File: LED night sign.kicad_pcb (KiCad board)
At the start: 2 copper layers, 42.9 x 36.7 mm, 24 parts, among them Q1 MOSFET-NCH-2N7002PW, U1 ATtiny85-20P, U2 ATtiny85-20S

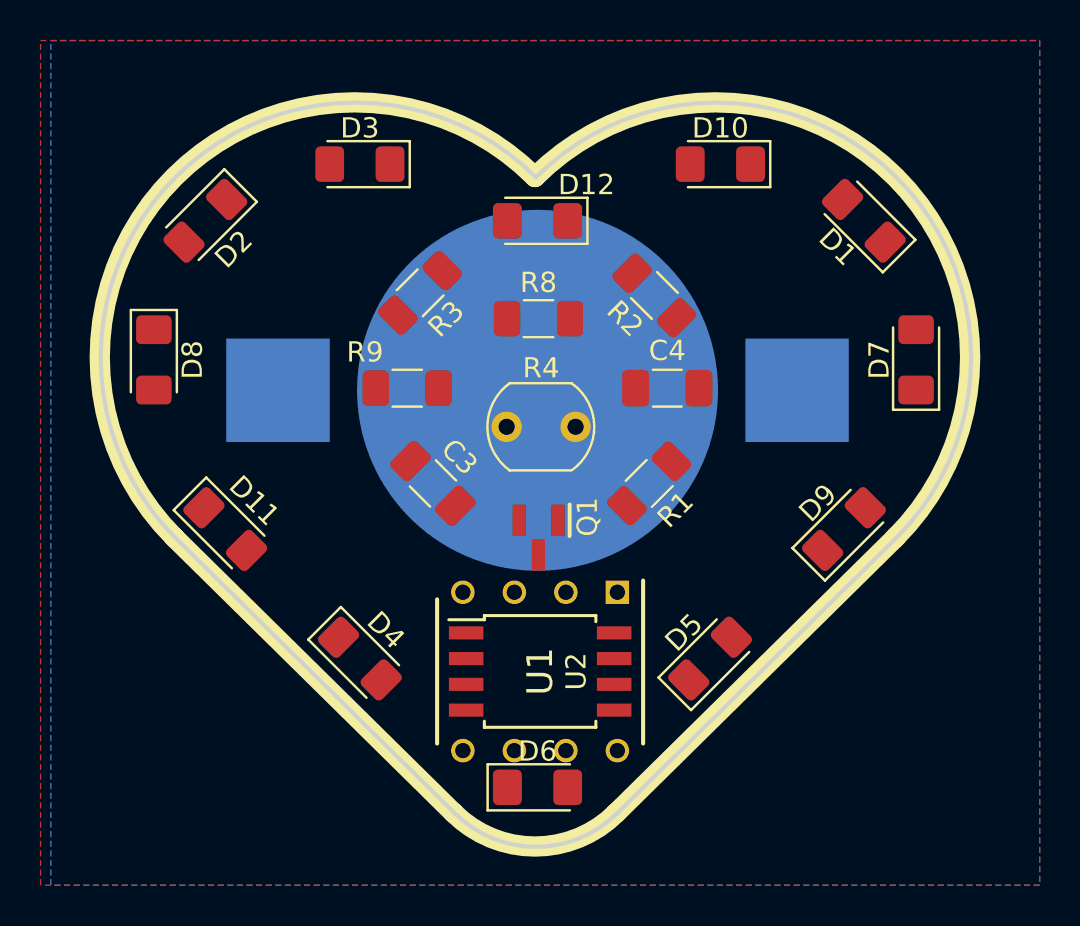
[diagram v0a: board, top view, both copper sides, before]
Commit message: moved components a bit down.
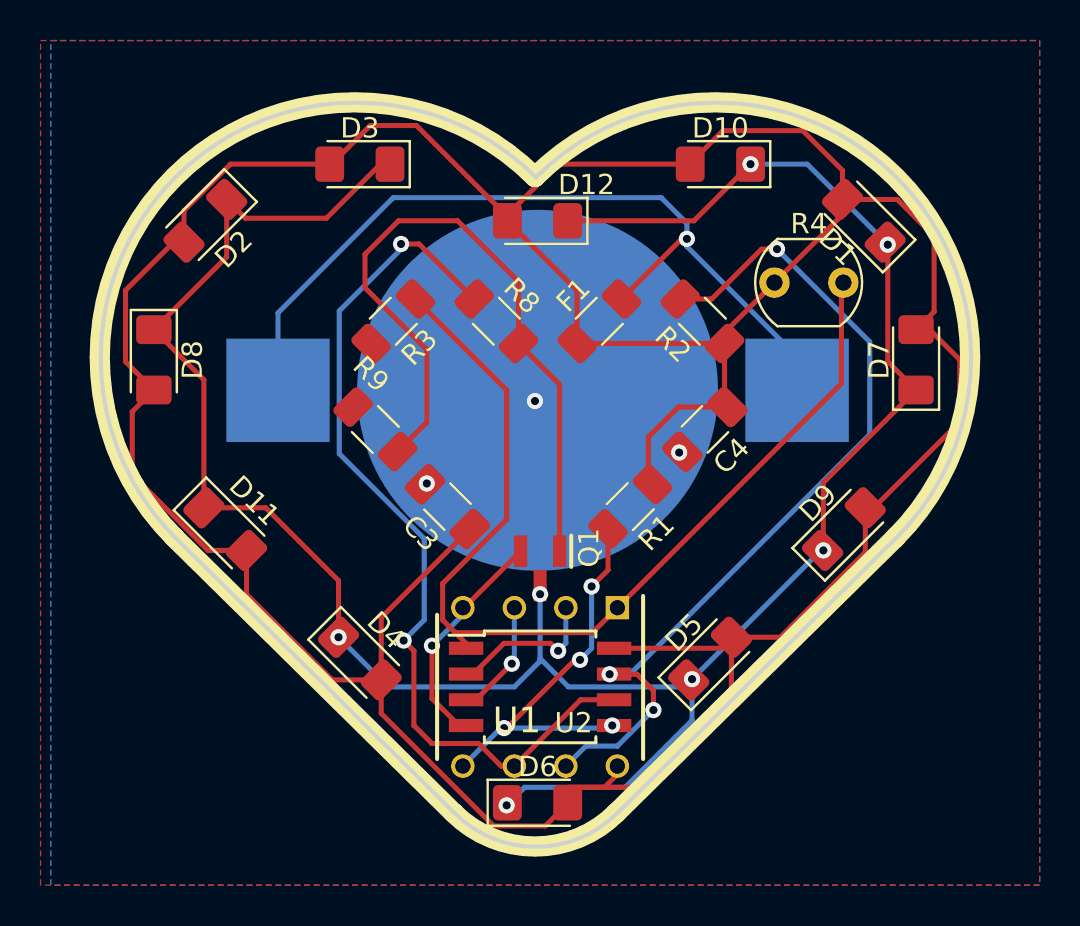
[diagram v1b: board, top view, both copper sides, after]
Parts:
- added F1: Fuse, Resistor_SMD:R_1206_3216Metric_Pad1.30x1.75mm_HandSolder, F.Cu at (153.0, 96.6)
- moved R4 15.0 mm to (161.7, 94.7)
- moved C4 2.75 mm to (158.2, 102.0), turned to -135 degrees
- moved R2 2.68 mm to (158.1, 96.6)
- moved R9 2.57 mm to (142.0, 102.0), turned to -45 degrees
- moved R8 2.08 mm to (148.0, 96.6), turned to 135 degrees
- moved R3 1.92 mm to (142.9, 96.6)
- moved Q1 1.53 mm to (150.1, 108.8)
- moved R1 1.48 mm to (154.6, 105.8)
- moved C3 1.35 mm to (145.5, 105.8), turned to 135 degrees
- moved D6 0.76 mm to (150.0, 120.4)
- moved U1 0.76 mm to (150.1, 114.7)
- moved U2 0.76 mm to (150.1, 114.7)
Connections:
- BT1 pad 1: +3V0 -> Net-(BT1-Pad1)
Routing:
- net +3V0: track 0.00 -> 186.0 mm
- net Net-(D1-Pad1): track 0.00 -> 119.5 mm, vias 0 -> 7
- net INTL: track 0.00 -> 50.0 mm
- net CTRLLED: track 0.00 -> 44.2 mm, vias 0 -> 2
- net PB2/SCL/SCK: track 0.00 -> 43.5 mm, vias 0 -> 3
- net Net-(BT1-Pad1): track 0.00 -> 41.8 mm, vias 0 -> 1
- net Net-(Q1-Pad1): track 0.00 -> 35.2 mm
- net PB0/SDA/MOSI: track 0.00 -> 20.4 mm, vias 0 -> 4
- net GND: track 0.00 -> 11.4 mm, vias 0 -> 4
- net unconnected-(U1-Pad2): track 0.00 -> 7.60 mm, vias 0 -> 1
- net PB4: track 0.00 -> 5.80 mm, vias 0 -> 1
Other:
- board text removed: "My heart beats unexpectedly when I think of you"

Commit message: centered components
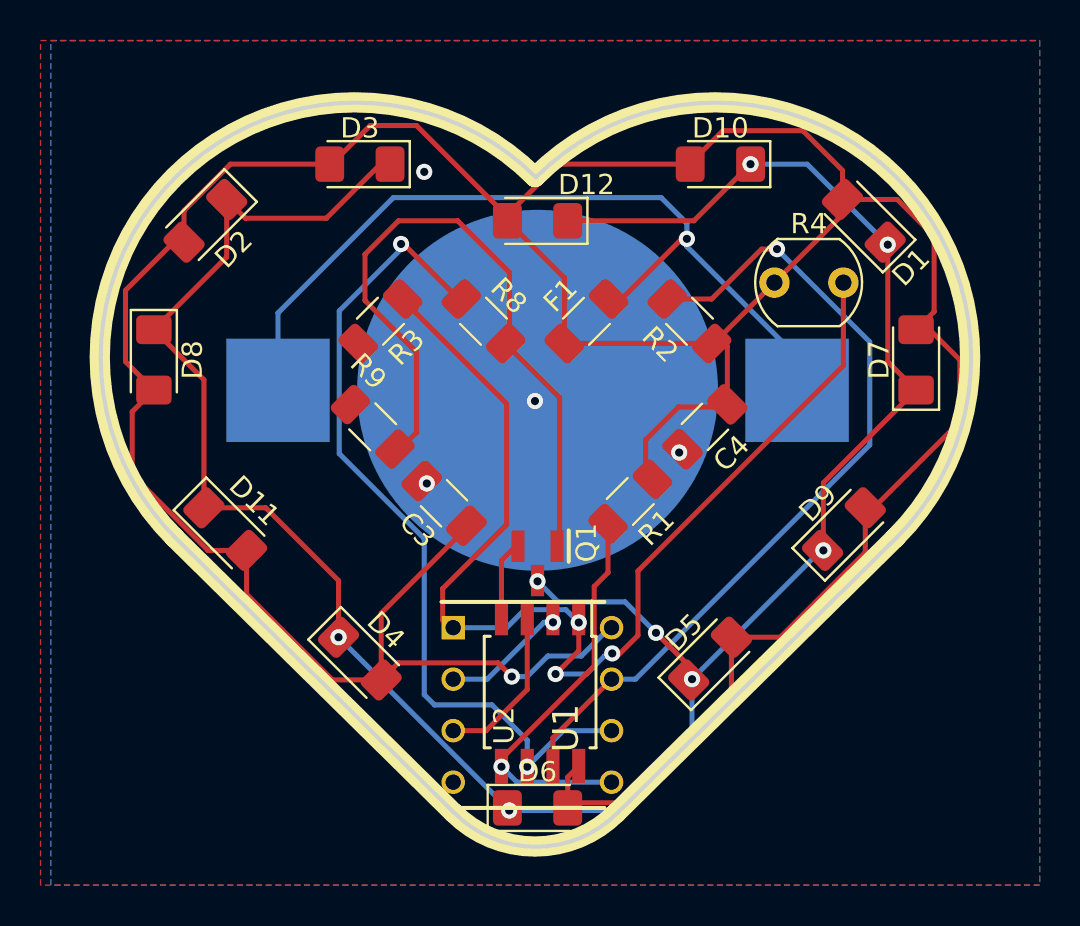
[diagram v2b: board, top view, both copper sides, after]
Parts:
- moved U1 0.97 mm to (149.7, 115.6), turned to 0 degrees
- moved R2 0.64 mm to (157.5, 96.6)
- moved R8 0.64 mm to (147.3, 96.6)
- moved F1 0.63 mm to (152.4, 96.6)
- moved R3 0.63 mm to (142.2, 96.6)
- moved Q1 0.28 mm to (150.0, 108.6)
- moved D6 0.25 mm to (150.0, 120.7)
- moved U2 0.25 mm to (150.1, 114.9), turned to -90 degrees
- moved R1 0.25 mm to (154.6, 105.5)
- moved C3 0.23 mm to (145.4, 105.6)
- moved R9 0.18 mm to (141.9, 101.9)
- moved C4 0.13 mm to (158.2, 101.9)
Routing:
- net GND: track 11.4 -> 4.07 mm
- net +3V0: track 186.0 -> 179.8 mm, vias 0 -> 1
- net INTL: track 50.0 -> 56.2 mm, vias 0 -> 3
- net PB2/SCL/SCK: track 43.5 -> 41.0 mm, vias 3 -> 1
- net CTRLLED: track 44.2 -> 42.2 mm
- net PB4: track 5.80 -> 7.76 mm, vias 1 -> 0
- net unconnected-(U1-Pad2): track 7.60 -> 6.08 mm
- net Net-(D1-Pad1): track 119.5 -> 118.7 mm, vias 7 -> 8
- net PB0/SDA/MOSI: track 20.4 -> 19.7 mm, vias 4 -> 1
- net Net-(BT1-Pad1): track 41.8 -> 42.4 mm

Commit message: added silkscreen
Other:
- board text added: "My hearth beats unexpectedly"
- board text added: "when i'm with you"
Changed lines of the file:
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@@
     (effects (font (size 1.5 1.5) (thickness 0.3)))
+  )
+  (gr_text "My hearth \nbeats unexpectedly \n" (at 165.1 91.44 -45) (layer "B.SilkS")
+    (effects (font (size 1.1 1.1) (thickness 0.15)) (justify mirror))
   )
   (gr_text "Designed by\nCasper R. Tak" (at 150.114 99.949) (layer "B.SilkS")
     (effects (font (size 0.9 0.9) (thickness 0.12)) (justify mirror))
   )
+  (gr_text "when i'm with you" (at 135.636 92.71 -315) (layer "B.SilkS")
+    (effects (font (size 1.1 1.1) (thickness 0.15)) (justify mirror))
+  )
   (gr_text "+\n" (at 161.29 103.505) (layer "B.SilkS")

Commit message: added push button
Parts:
- added R5: 10k, Resistor_SMD:R_1206_3216Metric_Pad1.30x1.75mm_HandSolder, F.Cu at (142.5, 108.7)
- added S1: MOMENTARY-SWITCH-SPST-2-SMD-5.2MM, Button_Switch_SMD:SW_SPST_TL3305B, F.Cu at (150.0, 101.7)
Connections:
- U1 pad 2: unconnected-(U1-Pad2) -> INTB
- U2 pad 2: unconnected-(U1-Pad2) -> INTB
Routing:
- net INTB: track 0.00 -> 28.6 mm, vias 0 -> 3
- net unconnected-(U1-Pad2): track 6.08 -> 0.00 mm, vias 1 -> 0
- net +3V0: track 179.8 -> 185.4 mm
- net CTRLLED: track 42.2 -> 41.4 mm
- net GND: vias 4 -> 6

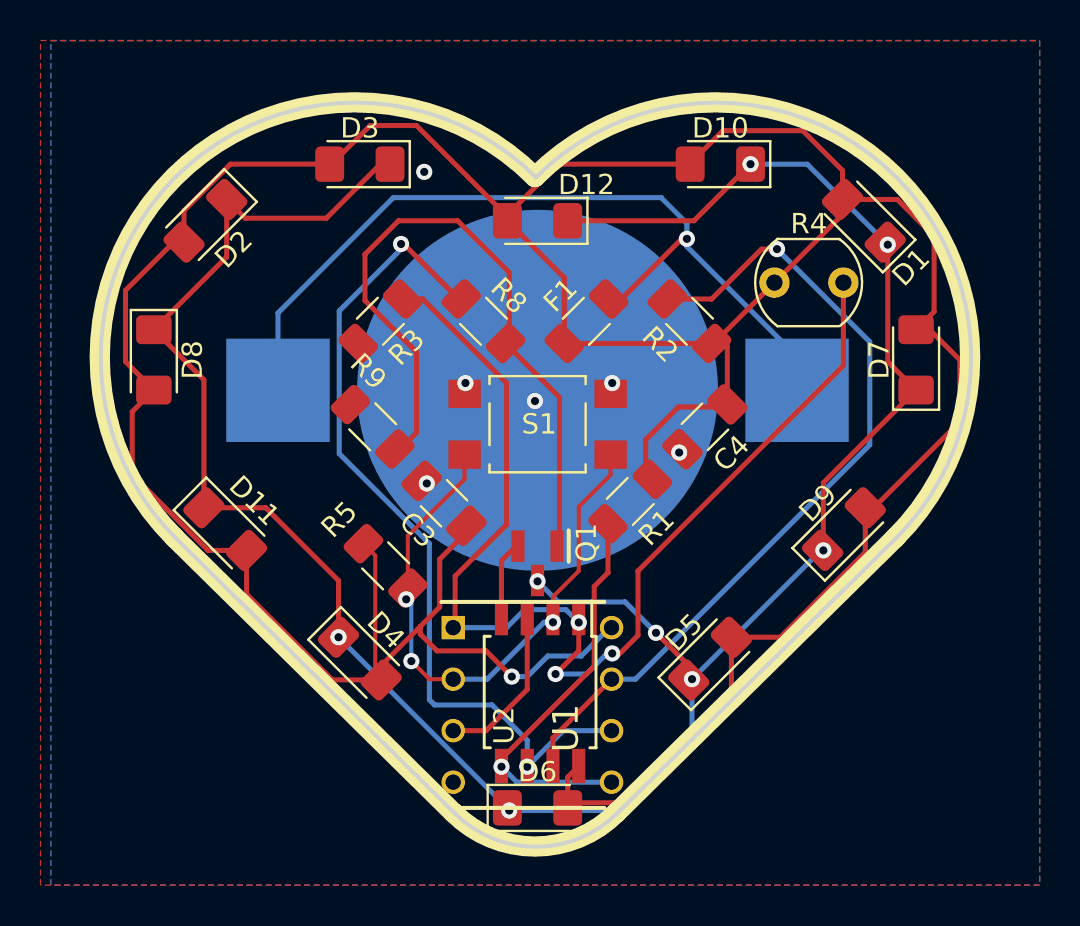
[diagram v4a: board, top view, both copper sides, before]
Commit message: added rounded traces and production
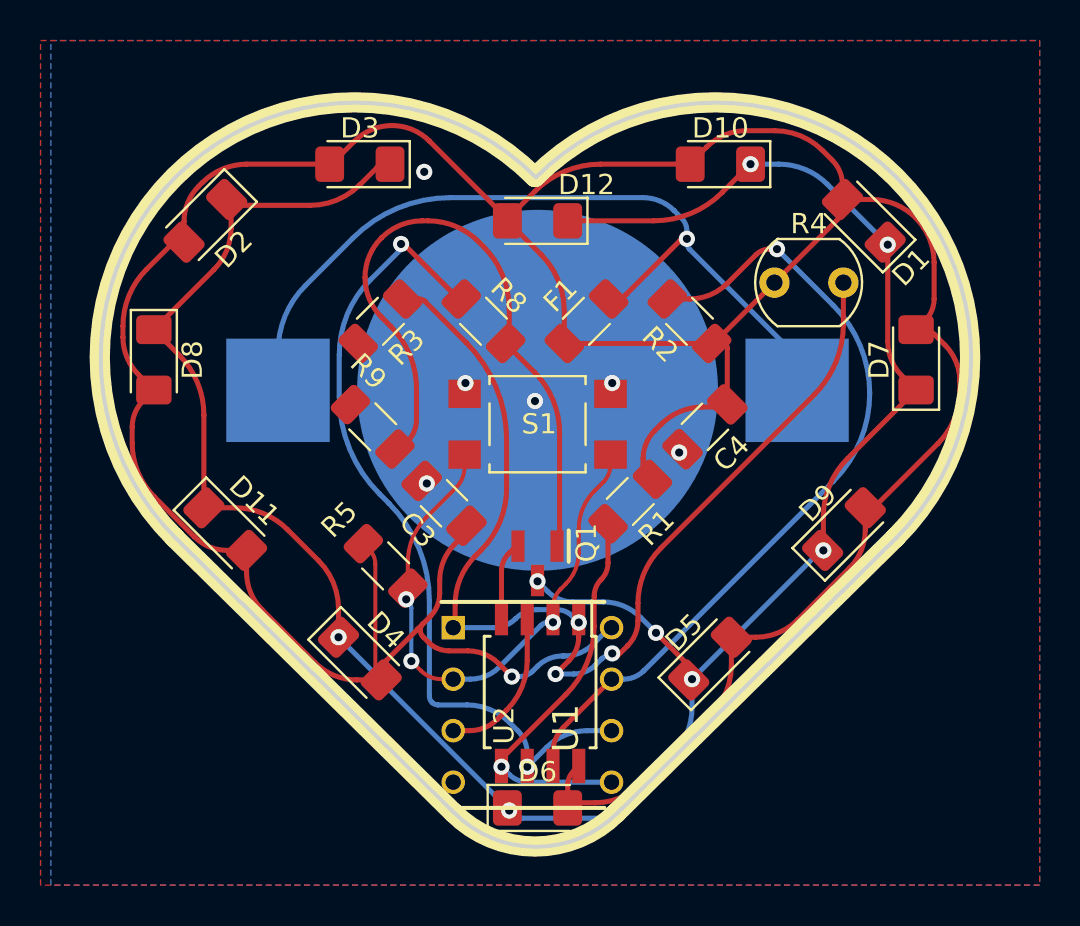
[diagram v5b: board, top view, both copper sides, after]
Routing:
- net +3V0: track 185.4 -> 181.6 mm
- net Net-(D1-Pad1): track 118.7 -> 116.4 mm
- net INTL: track 55.8 -> 54.3 mm
- net CTRLLED: track 41.4 -> 40.1 mm
- net Net-(Q1-Pad1): track 34.8 -> 33.5 mm
- net PB2/SCL/SCK: track 41.0 -> 40.1 mm
- net Net-(BT1-Pad1): track 42.4 -> 41.6 mm
- net INTB: track 28.6 -> 27.9 mm

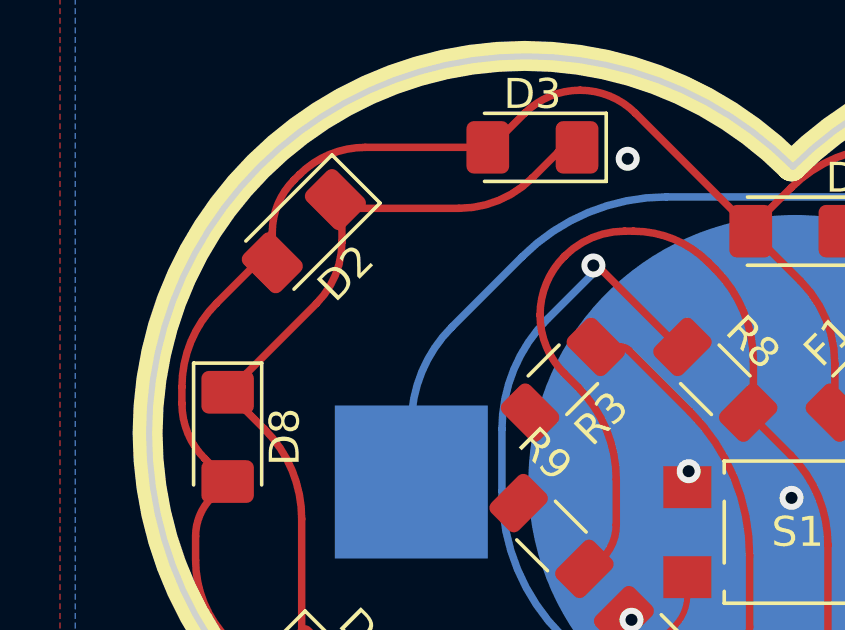
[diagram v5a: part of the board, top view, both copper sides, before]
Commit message: added mounting hole (for keychain)
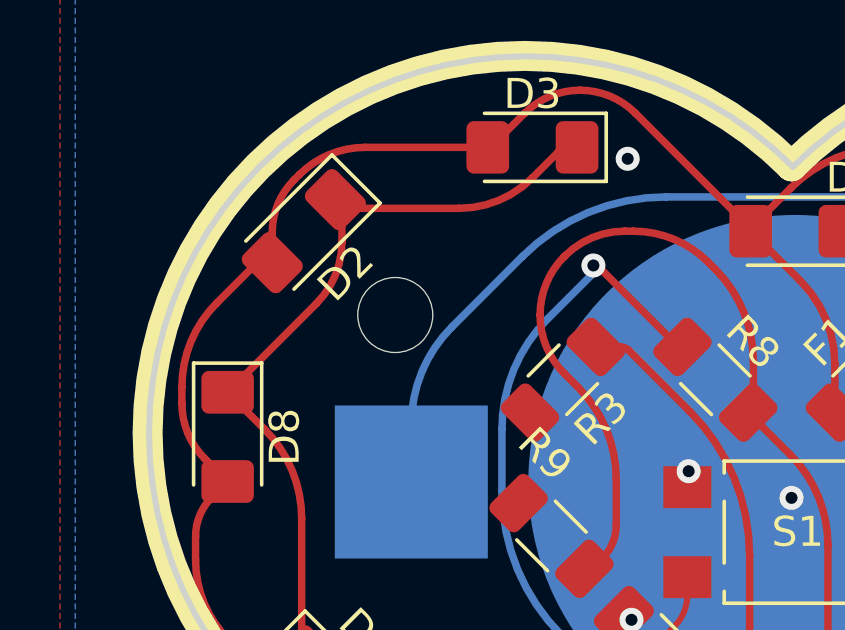
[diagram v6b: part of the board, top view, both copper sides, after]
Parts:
- added H1: MountingHole, MountingHole:MountingHole_2.5mm, F.Cu at (136.7, 94.5)
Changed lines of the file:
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@@
     )
+  )
+  (footprint "MountingHole:MountingHole_2.5mm" (layer "F.Cu")
+    (at 136.652 94.488)
+    (descr "Mounting Hole 2.5mm, no annular")
+    (tags "mounting hole 2.5mm no annular")
+    (property "Sheetfile" "LED night sign.kicad_sch")
+    (property "Sheetname" "")
+    (attr exclude_from_pos_files)
+    (fp_text reference "H1" (at 0 -3.5) (layer "F.SilkS") hide
+      (effects (font (size 1 1) (thickness 0.15)))
+    )
+    (fp_text value "MountingHole" (at 0 3.5) (layer "F.Fab")
+      (effects (font (size 1 1) (thickness 0.15)))
+    )
+    (fp_text user "${REFERENCE}" (at 0 0) (layer "F.Fab")
+      (effects (font (size 1 1) (thickness 0.15)))
+    )
+    (fp_circle (center 0 0) (end 2.5 0) (layer "Cmts.User") (width 0.15) (fill none))
+    (fp_circle (center 0 0) (end 2.75 0) (layer "F.CrtYd") (width 0.05) (fill none))
+    (pad "" np_thru_hole circle (at 0 0) (size 2.5 2.5) (drill 2.5) (layers *.Cu *.Mask))
   )
   (footprint "Button_Switch_SMD:SW_SPST_TL3305B" (layer "F.Cu")
